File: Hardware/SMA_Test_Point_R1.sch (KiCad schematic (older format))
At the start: 2 parts

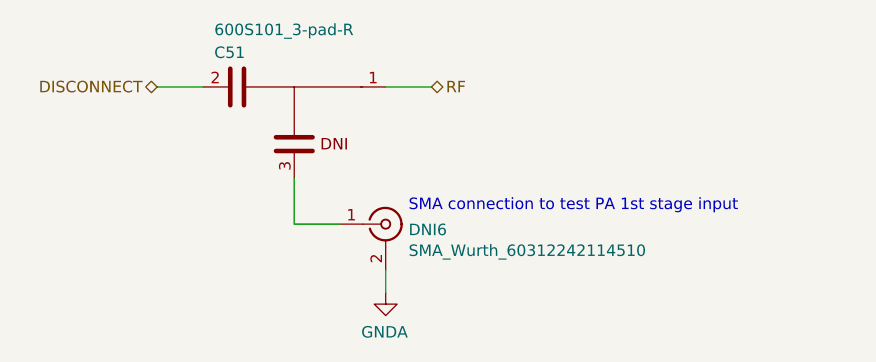
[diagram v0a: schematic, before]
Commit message: Improving LNA simulations and Documentation package. More to come on this one.
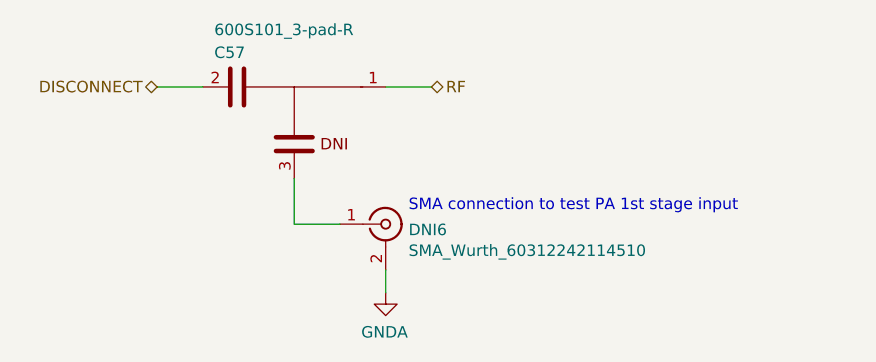
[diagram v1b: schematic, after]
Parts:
- renumbered C15 to C18
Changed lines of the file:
@@
 $Descr A4 11693 8268
 encoding utf-8
-Sheet 19 24
+Sheet 23 23
 Title ""
 Date ""
@@
 AR Path="/5F20DB0B/5F1BAF3E" Ref="#PWR?"  Part="1"
 AR Path="/5F2751D2/5F1BAF3E" Ref="#PWR?"  Part="1"
-AR Path="/5F2751D2/5F1B84EC/5F1BAF3E" Ref="#PWR018"  Part="1"
+AR Path="/5F2751D2/5F1B84EC/5F1BAF3E" Ref="#PWR020"  Part="1"
 AR Path="/5F19BA77/5F1C225B/5F1BAF3E" Ref="#PWR?"  Part="1"
 AR Path="/5F04F5B6/5F1AE89A/5F1CD1BB/5F1BAF3E" Ref="#PWR?"  Part="1"
@@
 AR Path="/5F1F7551/5F1BAF3E" Ref="#PWR?"  Part="1"
 AR Path="/5F204DEC/5F205D8E/5F1AE89A/5F1CD1BB/5F1BAF3E" Ref="#PWR?"  Part="1"
-AR Path="/5F204DEC/5F205D9E/5F1BAF3E" Ref="#PWR062"  Part="1"
-AR Path="/5F204DEC/5F205D8E/5F1B5FBD/5F1BAF3E" Ref="#PWR051"  Part="1"
-F 0 "#PWR062" H 6050 4200 50  0001 C CNN
+AR Path="/5F204DEC/5F205D9E/5F1BAF3E" Ref="#PWR066"  Part="1"
+AR Path="/5F204DEC/5F205D8E/5F1B5FBD/5F1BAF3E" Ref="#PWR053"  Part="1"
+F 0 "#PWR066" H 6050 4200 50  0001 C CNN
 F 1 "GNDA" H 6055 4277 50  0000 C CNN
 F 2 "" H 6050 4450 50  0001 C CNN
@@
 P 5650 3550
 AR Path="/5F2751D2/5F1BAF46" Ref="C?"  Part="1"
-AR Path="/5F2751D2/5F1B84EC/5F1BAF46" Ref="C15"  Part="1"
+AR Path="/5F2751D2/5F1B84EC/5F1BAF46" Ref="C18"  Part="1"
 AR Path="/5F19BA77/5F1C225B/5F1BAF46" Ref="C?"  Part="1"
 AR Path="/5F04F5B6/5F1AE89A/5F1CD1BB/5F1BAF46" Ref="C?"  Part="1"
@@
 AR Path="/5F1F7551/5F1BAF46" Ref="C?"  Part="1"
 AR Path="/5F204DEC/5F205D8E/5F1AE89A/5F1CD1BB/5F1BAF46" Ref="C?"  Part="1"
-AR Path="/5F204DEC/5F205D9E/5F1BAF46" Ref="C51"  Part="1"
-AR Path="/5F204DEC/5F205D8E/5F1B5FBD/5F1BAF46" Ref="C43"  Part="1"
-F 0 "C51" H 5300 3700 50  0000 L CNN
+AR Path="/5F204DEC/5F205D9E/5F1BAF46" Ref="C57"  Part="1"
+AR Path="/5F204DEC/5F205D8E/5F1B5FBD/5F1BAF46" Ref="C46"  Part="1"
+F 0 "C57" H 5300 3700 50  0000 L CNN
 F 1 "600S101_3-pad-R" H 5300 3800 50  0000 L CNN
 F 2 "Capacitor_SMD:C_0603_1608Metric_3-pad-R" H 6550 2800 50  0001 C CNN
